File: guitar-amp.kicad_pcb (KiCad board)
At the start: 2 copper layers, 3 parts, among them U1 ECC81, U2 ECC81, U3 EL84

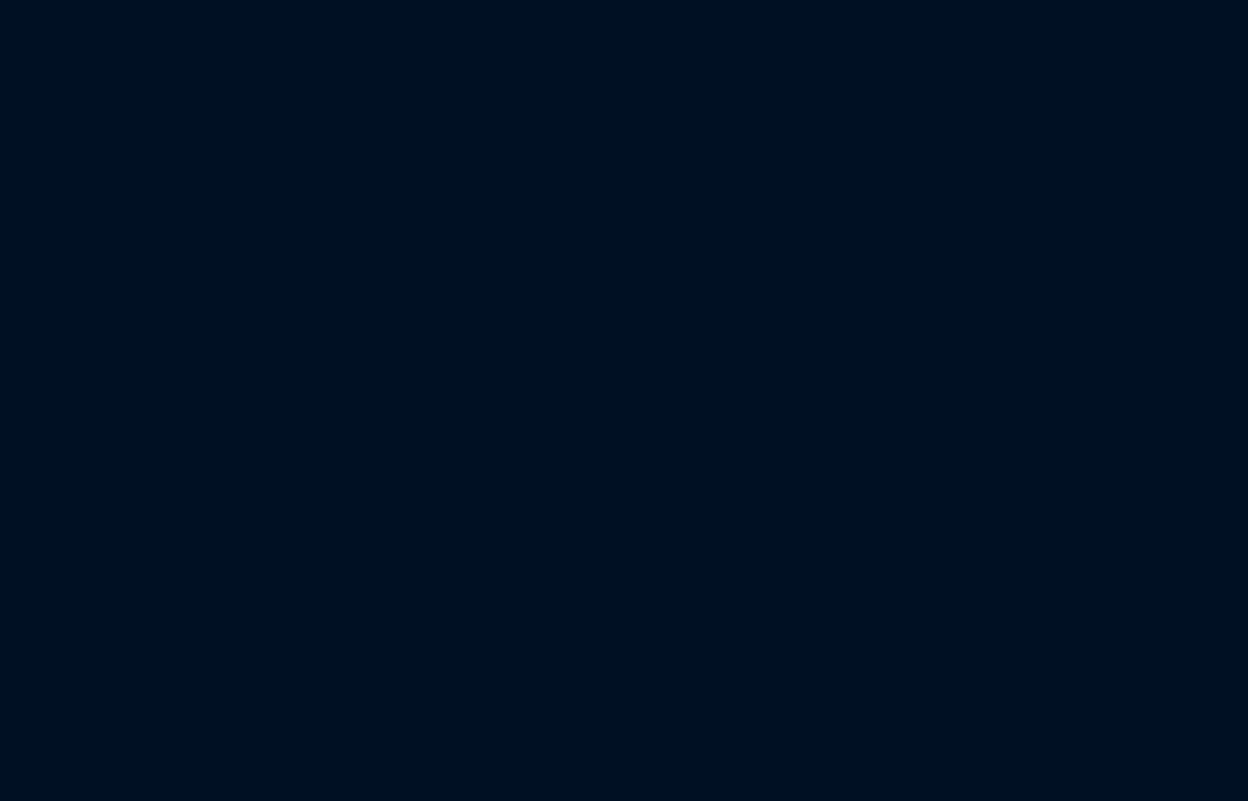
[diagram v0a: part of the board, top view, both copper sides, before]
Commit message: Add resistors
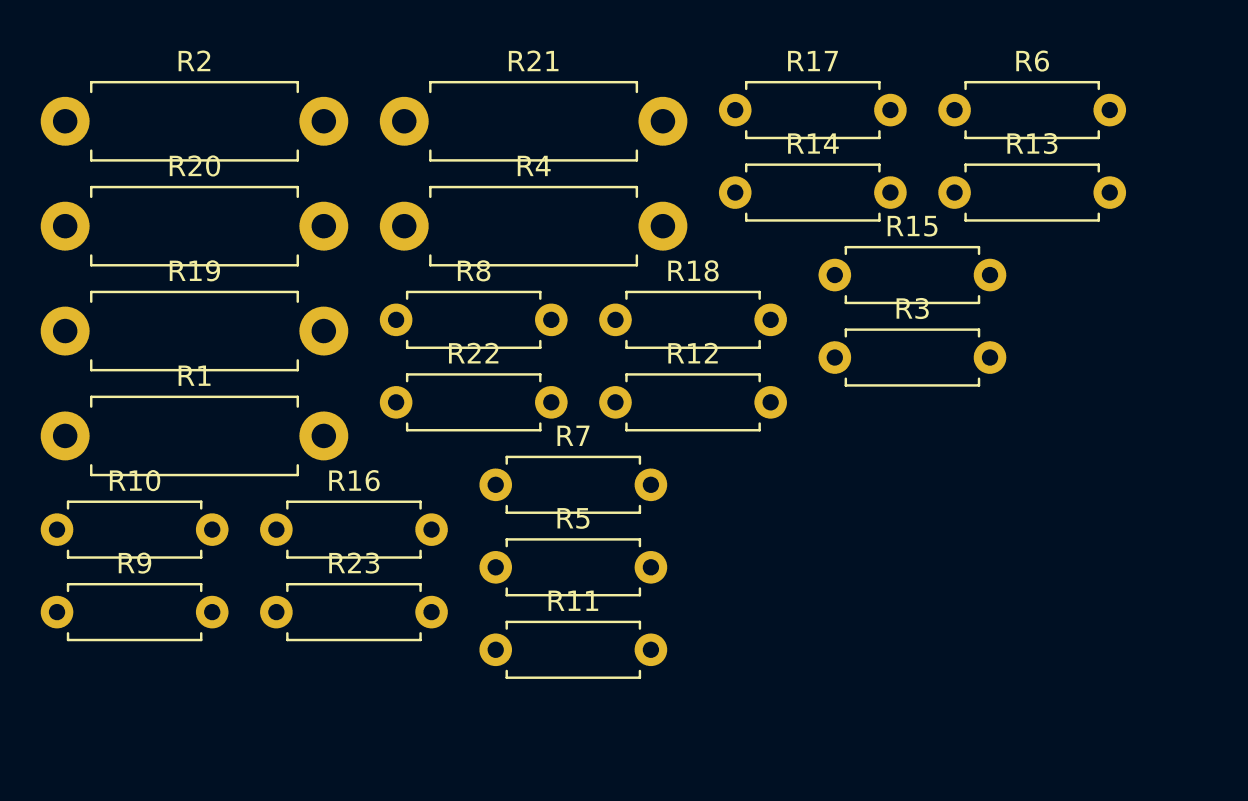
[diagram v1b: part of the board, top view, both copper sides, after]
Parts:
- added R1: R, Resistor_THT:R_Axial_DIN0411_L9.9mm_D3.6mm_P12.70mm_Horizontal, F.Cu at (47.0, 37.0)
- added R10: R, Resistor_THT:R_Axial_DIN0207_L6.3mm_D2.5mm_P7.62mm_Horizontal, F.Cu at (46.6, 41.6)
- added R11: R, Resistor_THT:R_Axial_DIN0207_L6.3mm_D2.5mm_P7.62mm_Horizontal, F.Cu at (68.1, 47.5)
- added R12: R, Resistor_THT:R_Axial_DIN0207_L6.3mm_D2.5mm_P7.62mm_Horizontal, F.Cu at (74.0, 35.4)
- added R13: R, Resistor_THT:R_Axial_DIN0207_L6.3mm_D2.5mm_P7.62mm_Horizontal, F.Cu at (90.7, 25.1)
- added R14: R, Resistor_THT:R_Axial_DIN0207_L6.3mm_D2.5mm_P7.62mm_Horizontal, F.Cu at (79.9, 25.1)
- added R15: R, Resistor_THT:R_Axial_DIN0207_L6.3mm_D2.5mm_P7.62mm_Horizontal, F.Cu at (84.8, 29.1)
- added R16: R, Resistor_THT:R_Axial_DIN0207_L6.3mm_D2.5mm_P7.62mm_Horizontal, F.Cu at (57.4, 41.6)
- added R17: R, Resistor_THT:R_Axial_DIN0207_L6.3mm_D2.5mm_P7.62mm_Horizontal, F.Cu at (79.9, 21.0)
- added R18: R, Resistor_THT:R_Axial_DIN0207_L6.3mm_D2.5mm_P7.62mm_Horizontal, F.Cu at (74.0, 31.3)
- added R19: R, Resistor_THT:R_Axial_DIN0411_L9.9mm_D3.6mm_P12.70mm_Horizontal, F.Cu at (47.0, 31.9)
- added R2: R, Resistor_THT:R_Axial_DIN0411_L9.9mm_D3.6mm_P12.70mm_Horizontal, F.Cu at (47.0, 21.6)
- added R20: R, Resistor_THT:R_Axial_DIN0411_L9.9mm_D3.6mm_P12.70mm_Horizontal, F.Cu at (47.0, 26.7)
- added R21: R, Resistor_THT:R_Axial_DIN0411_L9.9mm_D3.6mm_P12.70mm_Horizontal, F.Cu at (63.6, 21.6)
- added R22: R, Resistor_THT:R_Axial_DIN0207_L6.3mm_D2.5mm_P7.62mm_Horizontal, F.Cu at (63.2, 35.4)
- added R23: R, Resistor_THT:R_Axial_DIN0207_L6.3mm_D2.5mm_P7.62mm_Horizontal, F.Cu at (57.4, 45.6)
- added R3: 100k, Resistor_THT:R_Axial_DIN0207_L6.3mm_D2.5mm_P7.62mm_Horizontal, F.Cu at (84.8, 33.1)
- added R4: R, Resistor_THT:R_Axial_DIN0411_L9.9mm_D3.6mm_P12.70mm_Horizontal, F.Cu at (63.6, 26.7)
- added R5: R, Resistor_THT:R_Axial_DIN0207_L6.3mm_D2.5mm_P7.62mm_Horizontal, F.Cu at (68.1, 43.5)
- added R6: R, Resistor_THT:R_Axial_DIN0207_L6.3mm_D2.5mm_P7.62mm_Horizontal, F.Cu at (90.7, 21.0)
- added R7: R, Resistor_THT:R_Axial_DIN0207_L6.3mm_D2.5mm_P7.62mm_Horizontal, F.Cu at (68.1, 39.4)
- added R8: R, Resistor_THT:R_Axial_DIN0207_L6.3mm_D2.5mm_P7.62mm_Horizontal, F.Cu at (63.2, 31.3)
- added R9: R, Resistor_THT:R_Axial_DIN0207_L6.3mm_D2.5mm_P7.62mm_Horizontal, F.Cu at (46.6, 45.6)

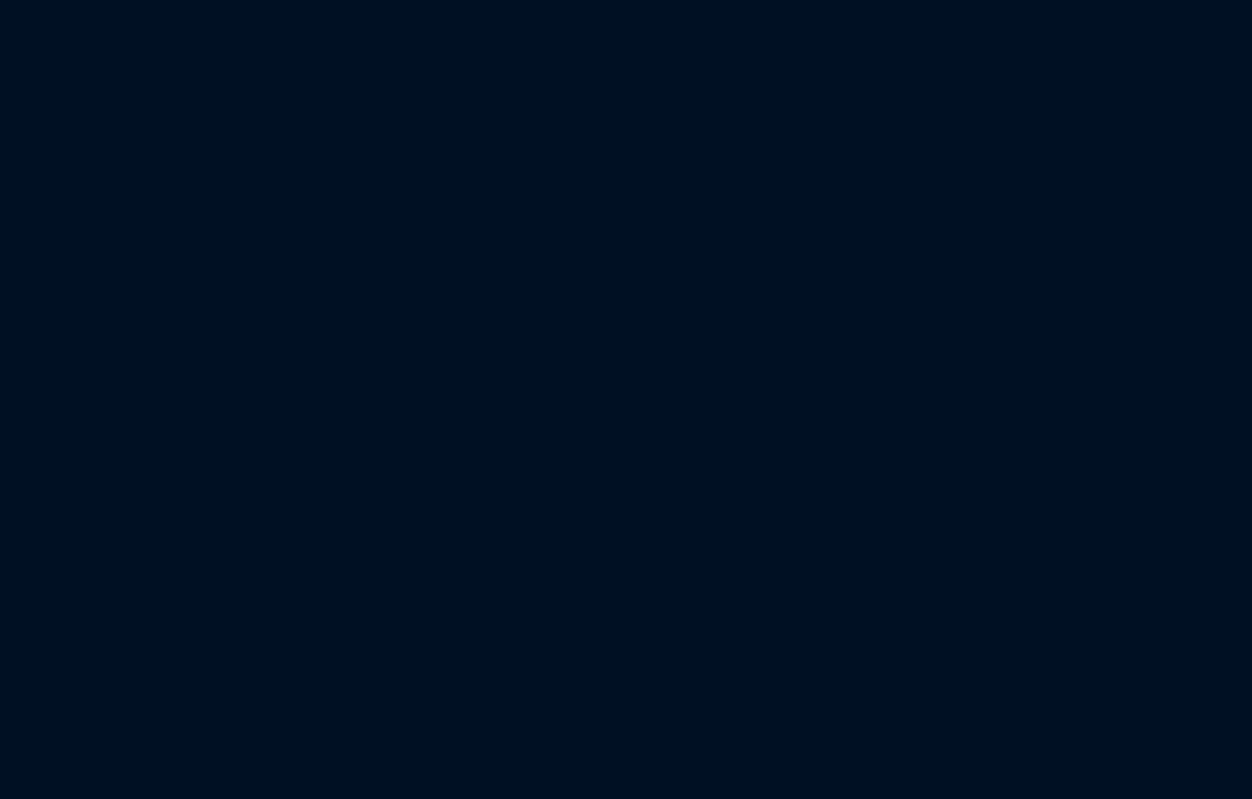
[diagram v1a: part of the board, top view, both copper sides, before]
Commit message: Add capacitors
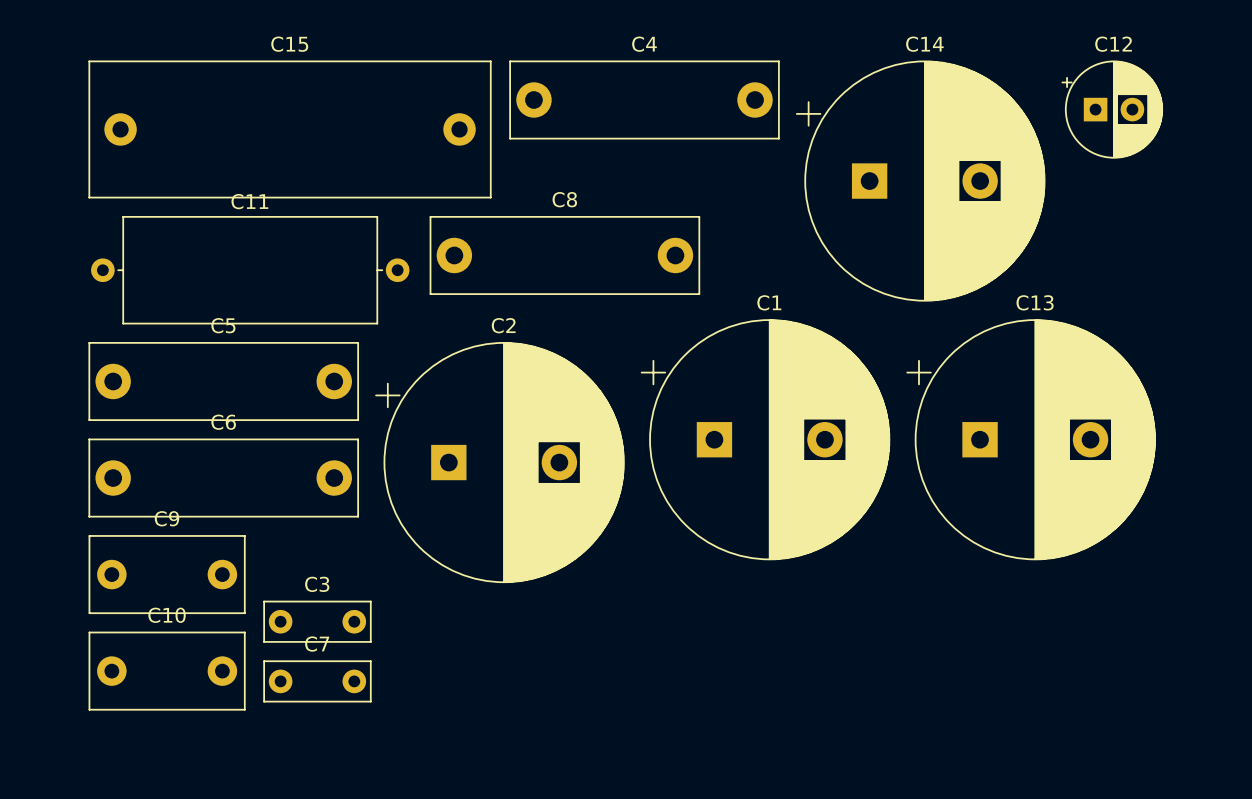
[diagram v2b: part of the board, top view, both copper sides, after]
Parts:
- added C1: 50u, Capacitor_THT:CP_Radial_D16.0mm_P7.50mm, F.Cu at (151.0, 44.0)
- added C10: 22n, Capacitor_THT:C_Rect_L10.3mm_W5.0mm_P7.50mm_MKS4, F.Cu at (110.1, 59.7)
- added C11: 680n, Capacitor_THT:C_Axial_L17.0mm_D7.0mm_P20.00mm_Horizontal, F.Cu at (109.5, 32.5)
- added C12: 50u, Capacitor_THT:CP_Radial_D6.3mm_P2.50mm, F.Cu at (176.9, 21.6)
- added C13: 50u, Capacitor_THT:CP_Radial_D16.0mm_P7.50mm, F.Cu at (169.0, 44.0)
- added C14: 50u, Capacitor_THT:CP_Radial_D16.0mm_P7.50mm, F.Cu at (161.5, 26.4)
- added C15: 1u / 250V, Capacitor_THT:C_Rect_L27.0mm_W9.0mm_P23.00mm, F.Cu at (110.7, 22.9)
- added C2: 50u, Capacitor_THT:CP_Radial_D16.0mm_P7.50mm, F.Cu at (133.0, 45.5)
- added C3: 470p, Capacitor_THT:C_Disc_D7.0mm_W2.5mm_P5.00mm, F.Cu at (121.6, 56.4)
- added C4: 22n, Capacitor_THT:C_Rect_L18.0mm_W5.0mm_P15.00mm_FKS3_FKP3, F.Cu at (138.8, 20.9)
- added C5: 22n, Capacitor_THT:C_Rect_L18.0mm_W5.0mm_P15.00mm_FKS3_FKP3, F.Cu at (110.2, 40.0)
- added C6: 22n, Capacitor_THT:C_Rect_L18.0mm_W5.0mm_P15.00mm_FKS3_FKP3, F.Cu at (110.2, 46.6)
- added C7: 470p, Capacitor_THT:C_Disc_D7.0mm_W2.5mm_P5.00mm, F.Cu at (121.6, 60.4)
- added C8: 22n, Capacitor_THT:C_Rect_L18.0mm_W5.0mm_P15.00mm_FKS3_FKP3, F.Cu at (133.4, 31.5)
- added C9: 22n, Capacitor_THT:C_Rect_L10.3mm_W5.0mm_P7.50mm_MKS4, F.Cu at (110.1, 53.1)
